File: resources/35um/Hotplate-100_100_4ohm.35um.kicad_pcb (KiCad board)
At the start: 2 copper layers, 100 x 100 mm, 7 parts, among them J1 Hotplate_Power_Connection, J2 Hotplate_Power_Connection

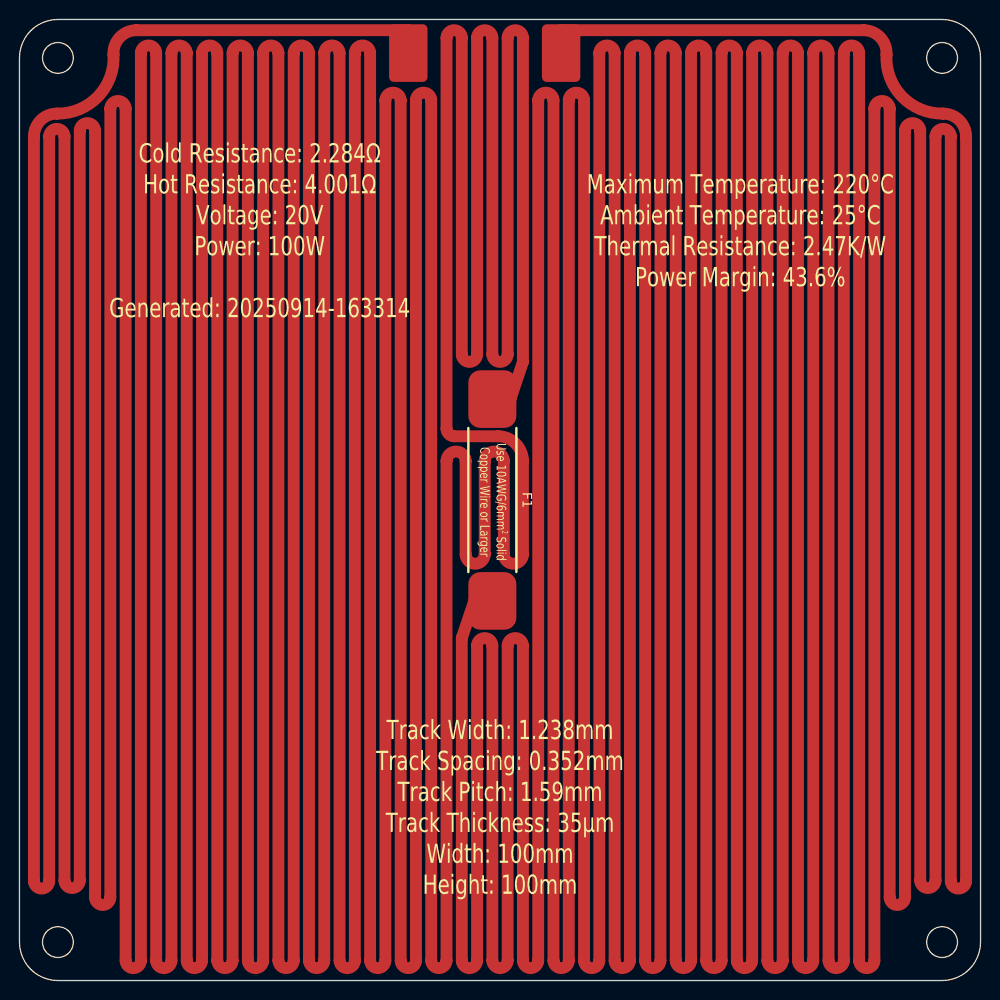
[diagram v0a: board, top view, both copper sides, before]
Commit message: Replaced obsolete 25mm thermal fuse footprint with new 35mm thermal fuse footprint.
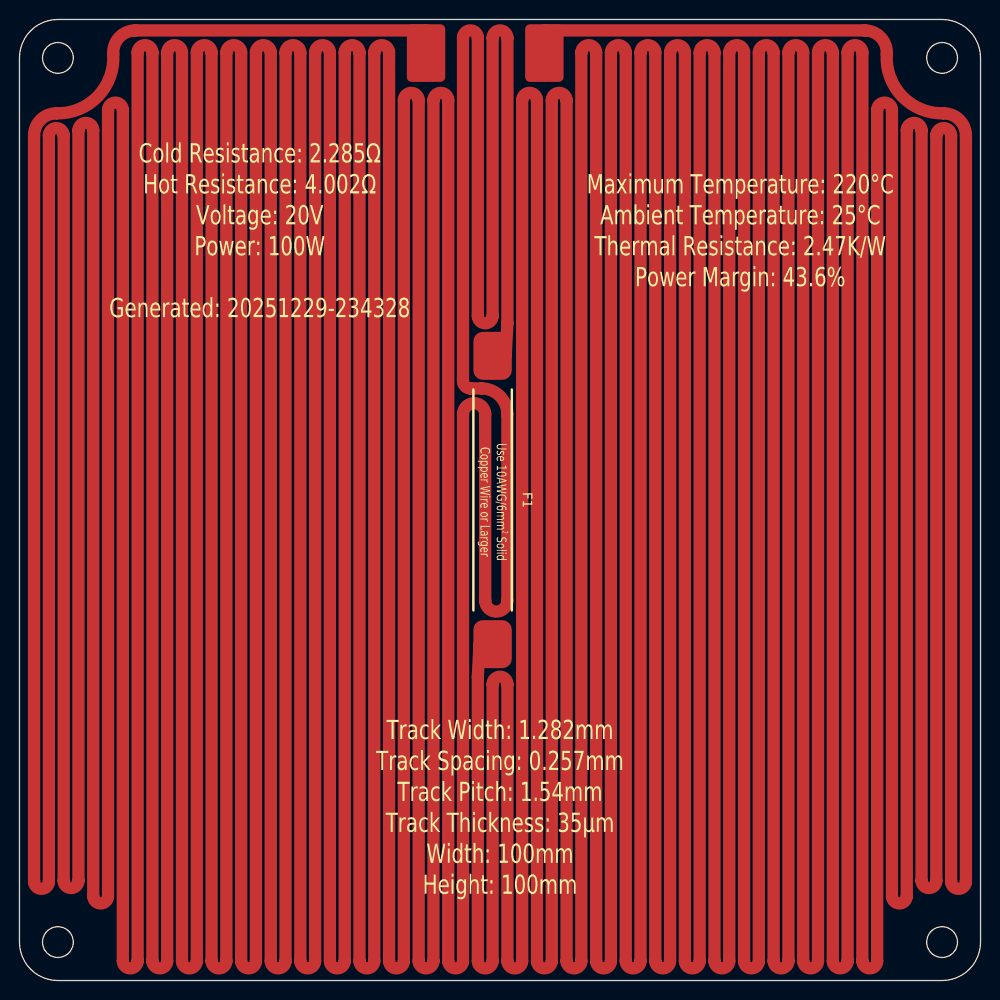
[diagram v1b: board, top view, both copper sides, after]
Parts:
- F1: footprint blg:Thermal Fuse, Front, 25mm -> blg:Thermal Fuse, SN100C, Front, 35mm
- moved J1 1.85 mm to (97.3, 58.5)
- moved J2 1.74 mm to (109.6, 58.5)
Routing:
- net Net-(J2-Pin_1): track 2913.3 -> 3025.2 mm
- net Net-(J1-Pin_1): track 2872.3 -> 2975.7 mm
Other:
- board text added: "Cold Resistance: 2.285Ω Hot Resistance: 4.002Ω Voltage: 20V Power: 100W Generated: 20251229-234328"
- board text added: "Track Width: 1.282mm Track Spacing: 0.257mm Track Pitch: 1.54mm Track Thickness: 35µm Width: 100mm Height: 100mm"
- board text removed: "Cold Resistance: 2.284Ω Hot Resistance: 4.001Ω Voltage: 20V Power: 100W Generated: 20250914-163314"
- board text removed: "Track Width: 1.238mm Track Spacing: 0.352mm Track Pitch: 1.59mm Track Thickness: 35µm Width: 100mm Height: 100mm"
